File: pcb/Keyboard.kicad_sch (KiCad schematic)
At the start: 63 parts

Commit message: wip
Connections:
- net GND: now also U_TRRS1.2 (TIP), U_TRRS2.2 (TIP); no longer U_TRRS1.3 (RING1), U_TRRS2.3 (RING1)
- net col0: now also U_PROMICRO1.9 (D7); no longer U_PROMICRO1.7 (D4)
- net col1: now also U_PROMICRO1.10 (E6); no longer U_PROMICRO1.8 (C6)
- net col2: now also U_PROMICRO1.11 (B4); no longer U_PROMICRO1.9 (D7)
- net col3: now also U_PROMICRO1.12 (B5); no longer U_PROMICRO1.10 (E6)
- net col4: now also U_PROMICRO1.17 (F7); no longer U_PROMICRO1.11 (B4)
- net col5: now also U_PROMICRO1.16 (B1); no longer U_PROMICRO1.12 (B5)
- net row0: now also U_PROMICRO1.7 (D4); no longer U_PROMICRO1.17 (F7)
- net row1: now also U_PROMICRO1.8 (C6); no longer U_PROMICRO1.16 (B1)
- net trrs: now also U_PROMICRO1.2 (RX), U_TRRS1.3 (RING1), U_TRRS2.3 (RING1); no longer U_PROMICRO1.6 (SCL), U_TRRS1.2 (TIP), U_TRRS2.2 (TIP)
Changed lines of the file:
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@@
   (no_connect (at 227.33 43.18))
   (no_connect (at 262.89 53.34))
-  (no_connect (at 262.89 45.72))
   (no_connect (at 262.89 43.18))
   (no_connect (at 227.33 58.42))
+  (no_connect (at 262.89 55.88))
   (no_connect (at 193.04 72.39))
   (no_connect (at 194.31 43.18))
@@
     (stroke (width 0) (type default) (color 0 0 0 0))
   )
-  (global_label "col5" (shape input) (at 262.89 71.12 0) (fields_autoplaced)
+  (global_label "col5" (shape input) (at 227.33 63.5 180) (fields_autoplaced)
+    (effects (font (size 1.27 1.27)) (justify right))
+    (property "Intersheet References" "${INTERSHEET_REFS}" (id 0) (at 220.8045 63.4206 0)
+      (effects (font (size 1.27 1.27)) (justify right) hide)
+    )
+  )
+  (global_label "col3" (shape input) (at 262.89 71.12 0) (fields_autoplaced)
     (effects (font (size 1.27 1.27)) (justify left))
     (property "Intersheet References" "${INTERSHEET_REFS}" (id 0) (at 269.4155 71.0406 0)
-      (effects (font (size 1.27 1.27)) (justify left) hide)
-    )
-  )
-  (global_label "col3" (shape input) (at 262.89 66.04 0) (fields_autoplaced)
-    (effects (font (size 1.27 1.27)) (justify left))
-    (property "Intersheet References" "${INTERSHEET_REFS}" (id 0) (at 269.4155 65.9606 0)
       (effects (font (size 1.27 1.27)) (justify left) hide)
     )
@@
     )
   )
-  (global_label "trrs" (shape input) (at 194.31 35.56 180) (fields_autoplaced)
+  (global_label "trrs" (shape input) (at 194.31 38.1 180) (fields_autoplaced)
     (effects (font (size 1.27 1.27)) (justify right))
-    (property "Intersheet References" "${INTERSHEET_REFS}" (id 0) (at 188.5707 35.4806 0)
+    (property "Intersheet References" "${INTERSHEET_REFS}" (id 0) (at 188.5707 38.0206 0)
       (effects (font (size 1.27 1.27)) (justify right) hide)
     )
@@
     )
   )
-  (global_label "trrs" (shape input) (at 262.89 55.88 0) (fields_autoplaced)
+  (global_label "trrs" (shape input) (at 262.89 45.72 0) (fields_autoplaced)
     (effects (font (size 1.27 1.27)) (justify left))
-    (property "Intersheet References" "${INTERSHEET_REFS}" (id 0) (at 268.6293 55.8006 0)
+    (property "Intersheet References" "${INTERSHEET_REFS}" (id 0) (at 268.6293 45.6406 0)
       (effects (font (size 1.27 1.27)) (justify left) hide)
     )
@@
     )
   )
-  (global_label "col2" (shape input) (at 262.89 63.5 0) (fields_autoplaced)
+  (global_label "col2" (shape input) (at 262.89 68.58 0) (fields_autoplaced)
     (effects (font (size 1.27 1.27)) (justify left))
-    (property "Intersheet References" "${INTERSHEET_REFS}" (id 0) (at 269.4155 63.4206 0)
+    (property "Intersheet References" "${INTERSHEET_REFS}" (id 0) (at 269.4155 68.5006 0)
       (effects (font (size 1.27 1.27)) (justify left) hide)
     )
@@
     )
   )
-  (global_label "col4" (shape input) (at 262.89 68.58 0) (fields_autoplaced)
-    (effects (font (size 1.27 1.27)) (justify left))
-    (property "Intersheet References" "${INTERSHEET_REFS}" (id 0) (at 269.4155 68.5006 0)
-      (effects (font (size 1.27 1.27)) (justify left) hide)
+  (global_label "col4" (shape input) (at 227.33 60.96 180) (fields_autoplaced)
+    (effects (font (size 1.27 1.27)) (justify right))
+    (property "Intersheet References" "${INTERSHEET_REFS}" (id 0) (at 220.8045 60.8806 0)
+      (effects (font (size 1.27 1.27)) (justify right) hide)
     )
   )
@@
     )
   )
-  (global_label "row0" (shape input) (at 227.33 60.96 180) (fields_autoplaced)
-    (effects (font (size 1.27 1.27)) (justify right))
-    (property "Intersheet References" "${INTERSHEET_REFS}" (id 0) (at 220.4417 60.8806 0)
-      (effects (font (size 1.27 1.27)) (justify right) hide)
+  (global_label "row0" (shape input) (at 262.89 58.42 0) (fields_autoplaced)
+    (effects (font (size 1.27 1.27)) (justify left))
+    (property "Intersheet References" "${INTERSHEET_REFS}" (id 0) (at 269.7783 58.3406 0)
+      (effects (font (size 1.27 1.27)) (justify left) hide)
     )
   )
@@
     )
   )
-  (global_label "col0" (shape input) (at 262.89 58.42 0) (fields_autoplaced)
+  (global_label "col0" (shape input) (at 262.89 63.5 0) (fields_autoplaced)
     (effects (font (size 1.27 1.27)) (justify left))
-    (property "Intersheet References" "${INTERSHEET_REFS}" (id 0) (at 269.4155 58.3406 0)
+    (property "Intersheet References" "${INTERSHEET_REFS}" (id 0) (at 269.4155 63.4206 0)
       (effects (font (size 1.27 1.27)) (justify left) hide)
     )
   )
-  (global_label "trrs" (shape input) (at 193.04 64.77 180) (fields_autoplaced)
+  (global_label "trrs" (shape input) (at 193.04 67.31 180) (fields_autoplaced)
     (effects (font (size 1.27 1.27)) (justify right))
-    (property "Intersheet References" "${INTERSHEET_REFS}" (id 0) (at 187.3007 64.6906 0)
+    (property "Intersheet References" "${INTERSHEET_REFS}" (id 0) (at 187.3007 67.2306 0)
       (effects (font (size 1.27 1.27)) (justify right) hide)
     )
   )
-  (global_label "row1" (shape input) (at 227.33 63.5 180) (fields_autoplaced)
-    (effects (font (size 1.27 1.27)) (justify right))
-    (property "Intersheet References" "${INTERSHEET_REFS}" (id 0) (at 220.4417 63.4206 0)
-      (effects (font (size 1.27 1.27)) (justify right) hide)
+  (global_label "row1" (shape input) (at 262.89 60.96 0) (fields_autoplaced)
+    (effects (font (size 1.27 1.27)) (justify left))
+    (property "Intersheet References" "${INTERSHEET_REFS}" (id 0) (at 269.7783 60.8806 0)
+      (effects (font (size 1.27 1.27)) (justify left) hide)
     )
   )
@@
     )
   )
-  (global_label "col1" (shape input) (at 262.89 60.96 0) (fields_autoplaced)
+  (global_label "col1" (shape input) (at 262.89 66.04 0) (fields_autoplaced)
     (effects (font (size 1.27 1.27)) (justify left))
-    (property "Intersheet References" "${INTERSHEET_REFS}" (id 0) (at 269.4155 60.8806 0)
+    (property "Intersheet References" "${INTERSHEET_REFS}" (id 0) (at 269.4155 65.9606 0)
       (effects (font (size 1.27 1.27)) (justify left) hide)
     )
@@
     (pin "1")
   )
-  (symbol (lib_id "power:GND") (at 193.04 67.31 270) (unit 1)
-    (in_bom yes) (on_board yes) (fields_autoplaced)
-    (property "Reference" "#PWR0102" (id 0) (at 186.69 67.31 0)
-      (effects (font (size 1.27 1.27)) hide)
-    )
-    (property "Value" "GND" (id 1) (at 189.23 67.3099 90)
-      (effects (font (size 1.27 1.27)) (justify right))
-    )
-    (property "Footprint" "" (id 2) (at 193.04 67.31 0)
-      (effects (font (size 1.27 1.27)) hide)
-    )
-    (property "Datasheet" "" (id 3) (at 193.04 67.31 0)
+  (symbol (lib_id "power:GND") (at 193.04 64.77 270) (unit 1)
+    (in_bom yes) (on_board yes)
+    (property "Reference" "#PWR0102" (id 0) (at 186.69 64.77 0)
+      (effects (font (size 1.27 1.27)) hide)
+    )
+    (property "Value" "GND" (id 1) (at 189.23 64.7699 90)
+      (effects (font (size 1.27 1.27)) (justify right))
+    )
+    (property "Footprint" "" (id 2) (at 193.04 64.77 0)
+      (effects (font (size 1.27 1.27)) hide)
+    )
+    (property "Datasheet" "" (id 3) (at 193.04 64.77 0)
       (effects (font (size 1.27 1.27)) hide)
     )
@@
     (pin "2")
   )
-  (symbol (lib_id "power:GND") (at 194.31 38.1 270) (unit 1)
-    (in_bom yes) (on_board yes) (fields_autoplaced)
-    (property "Reference" "#PWR0104" (id 0) (at 187.96 38.1 0)
-      (effects (font (size 1.27 1.27)) hide)
-    )
-    (property "Value" "GND" (id 1) (at 190.5 38.0999 90)
-      (effects (font (size 1.27 1.27)) (justify right))
-    )
-    (property "Footprint" "" (id 2) (at 194.31 38.1 0)
-      (effects (font (size 1.27 1.27)) hide)
-    )
-    (property "Datasheet" "" (id 3) (at 194.31 38.1 0)
-      (effects (font (size 1.27 1.27)) hide)
-    )
+  (symbol (lib_id "power:GND") (at 194.31 35.56 270) (unit 1)
+    (in_bom yes) (on_board yes) (fields_autoplaced)
+    (property "Reference" "#PWR0104" (id 0) (at 187.96 35.56 0)
+      (effects (font (size 1.27 1.27)) hide)
+    )
+    (property "Value" "GND" (id 1) (at 190.5 35.5599 90)
+      (effects (font (size 1.27 1.27)) (justify right))
+    )
+    (property "Footprint" "" (id 2) (at 194.31 35.56 0)
+      (effects (font (size 1.27 1.27)) hide)
+    )
+    (property "Datasheet" "" (id 3) (at 194.31 35.56 0)
+      (effects (font (size 1.27 1.27)) hide)
+    )

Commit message: wip
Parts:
- removed D_0_4, D_1_4, D_3_4, D_4_4, D_5_4: D, keyboard_parts:D_SOD123, symbol Device:D
- removed K_0_4, K_0_4_1, K_1_4, K_3_4, K_3_4_1, K_4_4, K_5_4: KEYSW, Switch_Keyboard_Hotswap_Kailh:SW_Hotswap_Kailh_Choc_V1_1.00u, symbol keyboard_parts:KEYSW
- removed U_PROMICRO1: ProMicro, promicro:ProMicro, symbol promicro:ProMicro
- removed U_TRRS1, U_TRRS2: TRRS, Keebio-Parts:TRRS-PJ-320A, symbol keebio:TRRS
- added D_0, D_6, D_7, D_8, D_9, D_ALT1, D_BSLS1, D_BSPC1, D_COMM1, D_DOT1, D_DOWN1, D_GUI1, D_H1, D_I1, D_J1, D_K1, D_L1, D_LEFT1, D_M1, D_N1, D_O1, D_P1, D_QUOT1, D_RAISE1, D_RGHT1, D_SCLN1, D_SLSH1, D_SPC1, D_TY1, D_U1, D_UP1, K_ENT1: D, keyboard_parts:D_SOD123, symbol Device:D
- added K_0, K_6, K_7, K_8, K_9, K_BSLS1, K_BSPC1, K_COMM1, K_DOT1, K_DOWN1, K_ENT2, K_H1, K_I1, K_J1, K_K1, K_L1, K_LALT1, K_LEFT1, K_LGUI1, K_M1, K_N1, K_O1, K_P1, K_QUOT1, K_RGHT1, K_RGUI1, K_SCLN1, K_SLSH1, K_SPC1, K_U1, K_UP1, K_Y1: KEYSW, Switch_Keyboard_Hotswap_Kailh:SW_Hotswap_Kailh_Choc_V1_1.00u, symbol keyboard_parts:KEYSW
- added U1: Elite-C, Keebio-Parts:Elite-C, symbol keebio:Elite-C
- renumbered D_1_0 to D_1, D_2_0 to D_2, D_3_0 to D_3, D_4_0 to D_4, D_5_0 to D_5, D_1_2 to D_A1, D_5_3 to D_B1, D_3_3 to D_C1, D_3_2 to D_D1, D_3_1 to D_E1, D_0_0 to D_ESC1, D_4_2 to D_F1, D_5_2 to D_G1, D_0_2 to D_LCTL1, D_1_1 to D_Q1, D_4_1 to D_R1, D_2_2 to D_S1, D_0_3 to D_SHIFT1, D_5_1 to D_T1, D_0_1 to D_TAB1, D_4_3 to D_V1, D_2_1 to D_W1, D_2_3 to D_X1, D_1_3 to D_Z1, K_1_0 to K_1, K_2_0 to K_2, K_3_0 to K_3, K_4_0 to K_4, K_5_0 to K_5, K_1_2 to K_A1, K_5_3 to K_B1, K_3_3 to K_C1, K_3_2 to K_D1, K_3_1 to K_E1, K_0_0 to K_ESC1, K_4_2 to K_F1, K_5_2 to K_G1, K_0_2 to K_LCTL1, K_0_3 to K_LSFT1, K_1_1 to K_Q1, K_4_1 to K_R1, K_2_2 to K_S1, K_5_1 to K_T1, K_0_1 to K_TAB1, K_4_3 to K_V1, K_2_1 to K_W1, K_2_3 to K_X1, K_1_3 to K_Z1
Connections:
- net GND: now also U1.23 (GND), U1.3 (GND), U1.4 (GND)
- net VCC: now also U1.21 (VCC)
- net col0: now also K_LALT1.1, U1.20 (A3/PF4)
- net col1: now also U1.19 (A2/PF5)
- net col2: now also U1.18 (A1/PF6)
- net col3: now also U1.17 (A0/PF7); no longer K_C1.1, K_D1.1
- net col4: now also U1.16 (15/PB1)
- net col5: now also K_SPC1.1, U1.15 (14/PB3)
- net row0: now also D_0.1 (K), D_6.1 (K), D_7.1 (K), D_8.1 (K), D_9.1 (K), D_BSLS1.2 (A), D_BSPC1.1 (K), K_BSLS1.2, U1.5 (2/PD1)
- net row1: now also D_BSLS1.1 (K), D_I1.1 (K), D_O1.1 (K), D_P1.1 (K), D_TY1.1 (K), D_U1.1 (K), U1.6 (3/PD0)
- net row2: now also D_H1.1 (K), D_J1.1 (K), D_K1.1 (K), D_L1.1 (K), D_QUOT1.1 (K), D_SCLN1.1 (K), U1.7 (4/PD4)
- net row3: now also D_COMM1.1 (K), D_DOT1.1 (K), D_M1.1 (K), D_N1.1 (K), D_SLSH1.1 (K), D_UP1.1 (K), U1.8 (5/PC6)
- net row4: now also D_ALT1.1 (K), D_DOWN1.1 (K), D_GUI1.1 (K), D_LEFT1.1 (K), D_RAISE1.1 (K), D_RGHT1.1 (K), D_SPC1.1 (K), K_ENT1.1 (K), U1.9 (6/PD7)
- new net: D_6.2 (A), K_6.2
- new net: D_ALT1.2 (A), K_LALT1.2
- new net: D_SPC1.2 (A), K_SPC1.2
- new net: D_U1.2 (A), K_U1.2
- new net: D_QUOT1.2 (A), K_QUOT1.2
- new net: D_LEFT1.2 (A), K_LEFT1.2
- new net: D_SLSH1.2 (A), K_SLSH1.2
- new net: D_O1.2 (A), K_O1.2
- new net: D_SCLN1.2 (A), K_SCLN1.2
- new net: D_TY1.2 (A), K_Y1.2
- new net: D_DOWN1.2 (A), K_DOWN1.2
- new net: D_H1.2 (A), K_H1.2
- new net: D_BSPC1.2 (A), K_BSPC1.2
- new net: D_M1.2 (A), K_M1.2
- new net: D_7.2 (A), K_7.2
- new net: D_8.2 (A), K_8.2
- new net: D_P1.2 (A), K_P1.2
- new net: D_UP1.2 (A), K_UP1.2
- new net: D_K1.2 (A), K_K1.2
- new net: K_C1.1, K_D1.1, K_LGUI1.1
- new net: D_RGHT1.2 (A), K_RGHT1.2
- new net: D_GUI1.2 (A), K_LGUI1.2
- new net: D_J1.2 (A), K_J1.2
- new net: D_I1.2 (A), K_I1.2
- new net: D_L1.2 (A), K_L1.2
- new net: D_RAISE1.2 (A), K_RGUI1.2
- new net: D_DOT1.2 (A), K_DOT1.2
- new net: D_COMM1.2 (A), K_COMM1.2
- new net: D_0.2 (A), K_0.2
- new net: D_9.2 (A), K_9.2
- new net: K_ENT1.2 (A), K_ENT2.2
- new net: D_N1.2 (A), K_N1.2
- new net col10: K_0.1, K_DOWN1.1, K_P1.1, K_SCLN1.1, K_SLSH1.1, U1.27 (C7)
- new net col11: K_BSLS1.1, K_BSPC1.1, K_QUOT1.1, K_RGHT1.1, K_UP1.1, U1.26 (D5)
- new net col6: K_6.1, K_ENT2.1, K_H1.1, K_N1.1, K_Y1.1, U1.14 (16/PB2)
- new net col7: K_7.1, K_J1.1, K_M1.1, K_RGUI1.1, K_U1.1, U1.13 (10/PB6)
- new net col8: K_8.1, K_COMM1.1, K_I1.1, K_K1.1, U1.29 (F0)
- new net col9: K_9.1, K_DOT1.1, K_L1.1, K_LEFT1.1, K_O1.1, U1.28 (F1)
- no-connect marks 10 -> 7
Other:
- moved on the sheet: D_1, D_2, D_3, D_4, D_5, D_A1, D_B1, D_C1, D_D1, D_E1, D_ESC1, D_F1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

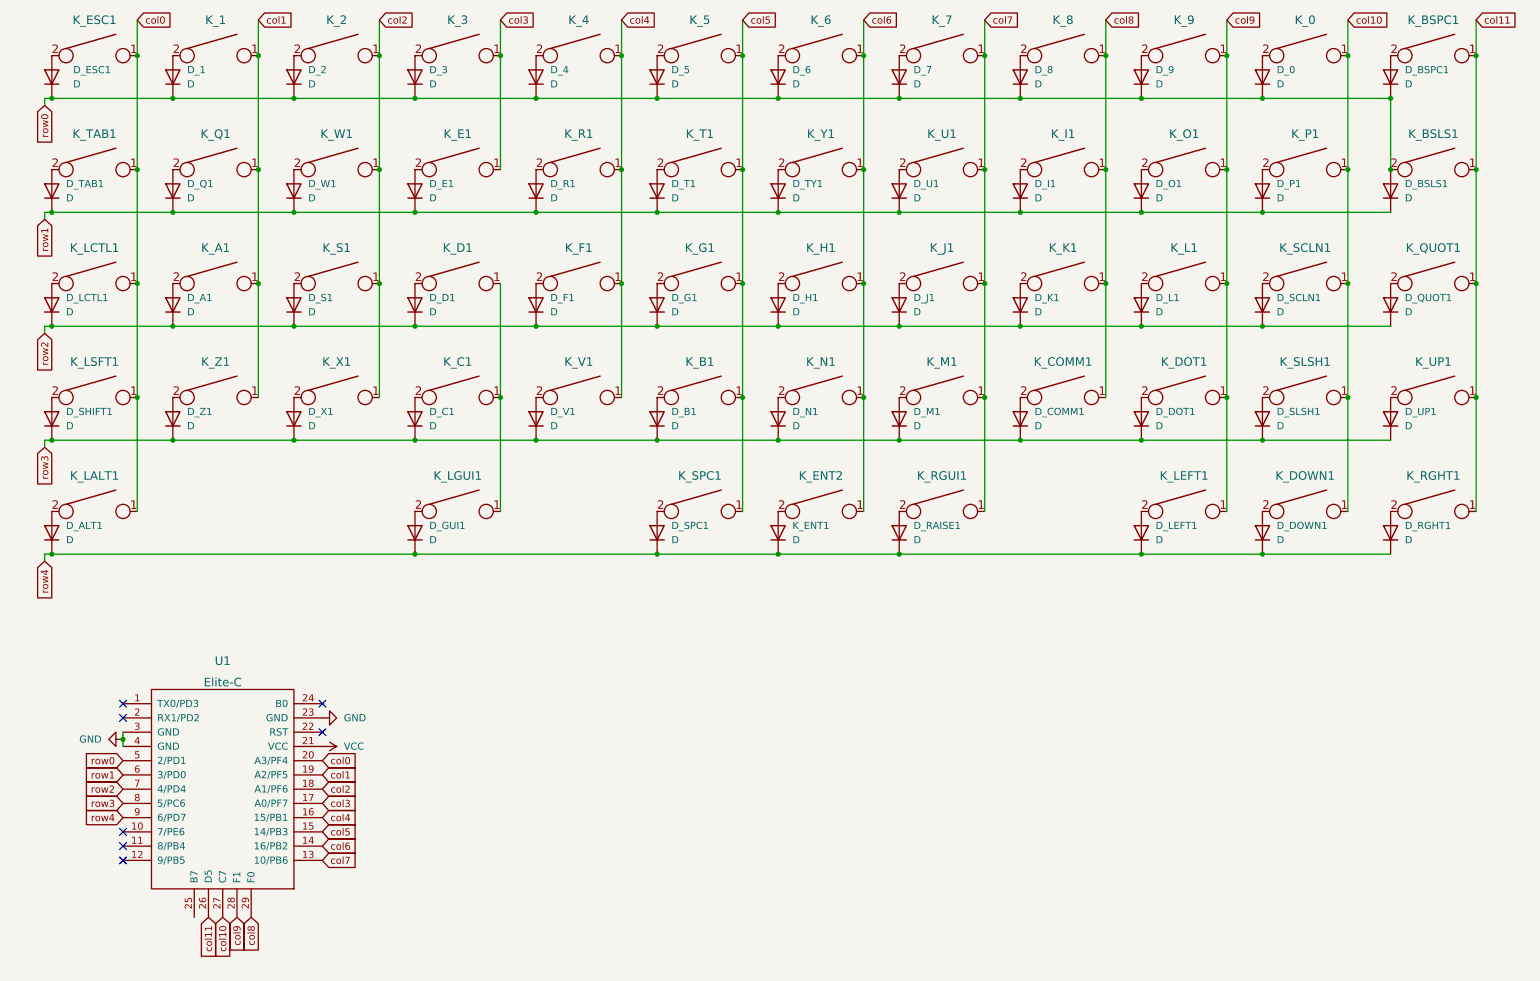
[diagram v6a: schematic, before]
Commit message: Low profile alice-like.
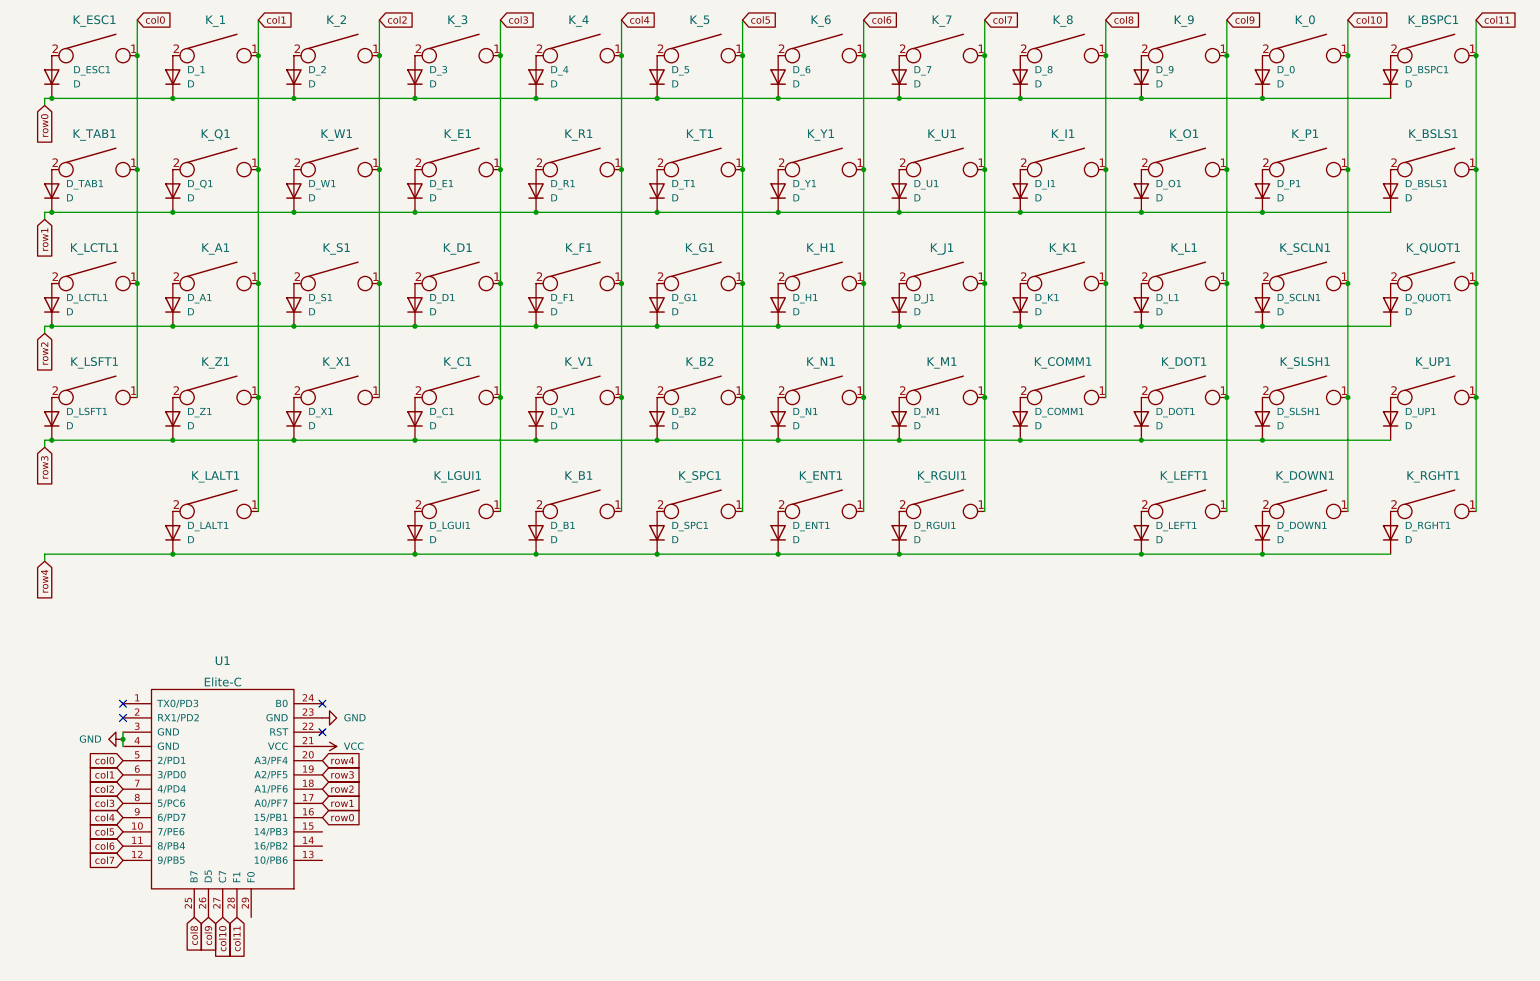
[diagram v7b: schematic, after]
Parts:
- added D_B1: D, keyboard_parts:D_SOD123, symbol Device:D
- added K_B1: KEYSW, Switch_Keyboard_Hotswap_Kailh:SW_Hotswap_Kailh_Choc_V1_1.00u, symbol keyboard_parts:KEYSW
- renumbered D_B1 to D_B2, K_ENT1 to D_ENT1, D_ALT1 to D_LALT1, D_GUI1 to D_LGUI1, D_SHIFT1 to D_LSFT1, D_RAISE1 to D_RGUI1, D_TY1 to D_Y1, K_B1 to K_B2, K_ENT2 to K_ENT1
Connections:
- net col0: now also U1.5 (2/PD1); no longer K_LALT1.1, U1.20 (A3/PF4)
- net col1: now also K_LALT1.1, U1.6 (3/PD0); no longer U1.19 (A2/PF5)
- net col11: now also U1.28 (F1); no longer U1.26 (D5)
- net col2: now also U1.7 (4/PD4); no longer U1.18 (A1/PF6)
- net col3: now also K_C1.1, K_D1.1, K_LGUI1.1, U1.8 (5/PC6); no longer U1.17 (A0/PF7)
- net col4: now also U1.9 (6/PD7), K_B1.1; no longer U1.16 (15/PB1)
- net col5: now also U1.10 (7/PE6); no longer U1.15 (14/PB3)
- net col6: now also U1.11 (8/PB4); no longer U1.14 (16/PB2)
- net col7: now also U1.12 (9/PB5); no longer U1.13 (10/PB6)
- net col8: now also U1.25 (B7); no longer U1.29 (F0)
- net col9: now also U1.26 (D5); no longer U1.28 (F1)
- net row0: now also U1.16 (15/PB1); no longer D_BSLS1.2 (A), K_BSLS1.2, U1.5 (2/PD1)
- net row1: now also U1.17 (A0/PF7); no longer U1.6 (3/PD0)
- net row2: now also U1.18 (A1/PF6); no longer U1.7 (4/PD4)
- net row3: now also U1.19 (A2/PF5); no longer U1.8 (5/PC6)
- net row4: now also U1.20 (A3/PF4), D_B1.1 (K); no longer U1.9 (6/PD7)
- new net: D_B1.2 (A), K_B1.2
- new net: D_BSLS1.2 (A), K_BSLS1.2
- no-connect marks 7 -> 4
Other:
- moved on the sheet: D_LALT1, K_LALT1
